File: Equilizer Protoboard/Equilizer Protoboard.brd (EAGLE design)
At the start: 14 parts, among them U1 ARDUINOR3-BPLACE

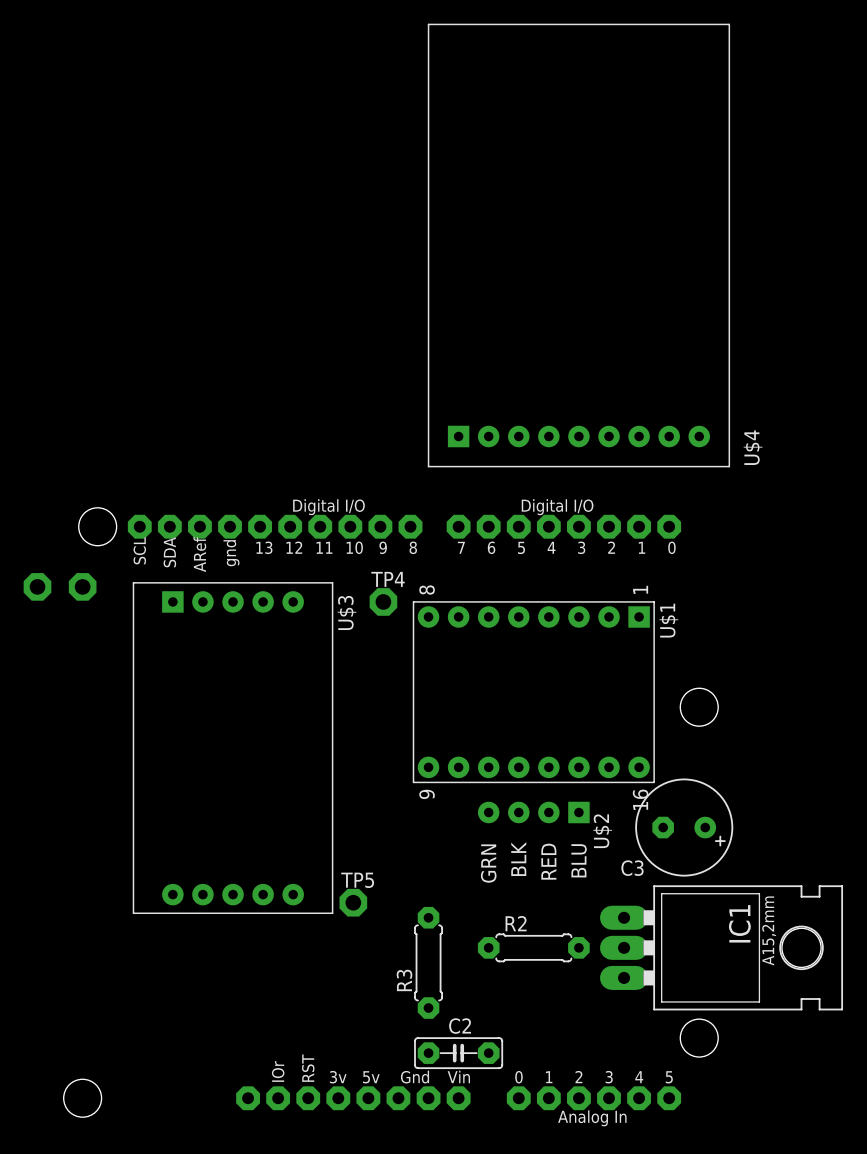
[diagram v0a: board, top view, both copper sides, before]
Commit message: Added Datalog Parser
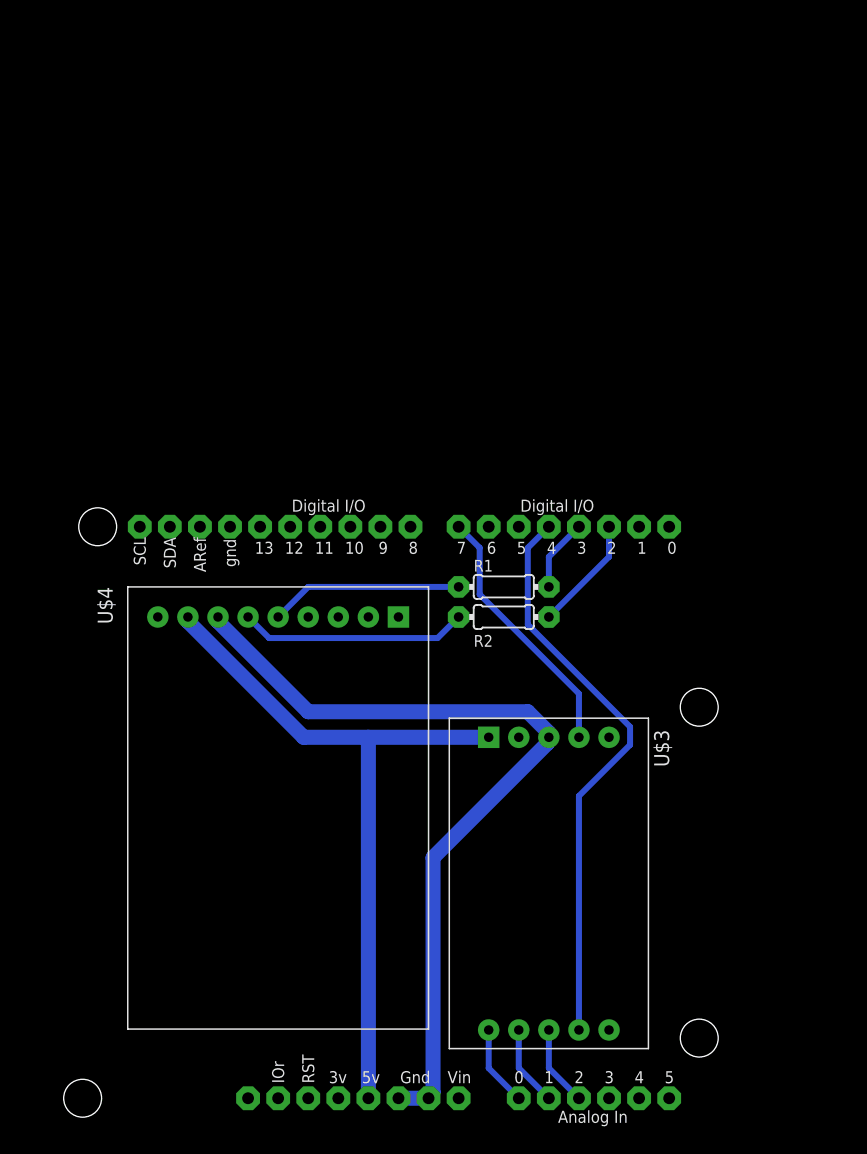
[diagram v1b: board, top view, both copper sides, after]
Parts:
- removed C2: 0.1uF, adafruit:C050-025X075
- removed C3: 1.0uF, adafruit:E3,5-8
- removed IC1: (no value), v-reg:317TL
- removed R3: 680, adafruit:0207/7
- removed TP11, TP12, TP4, TP5: TPPAD1-13, testpad:P1-13
- removed U$1: A4988, custom:A4988
- removed U$2: POLOLU_STEPPER, custom:POLOLU_STEPPER
- added R1: 0, adafruit:0204/7
- R2: value 330 -> 0; device adafruit:0207/7 -> adafruit:0204/7
- U1: device custom:ARDUINOR3-BPLACE -> adafruit:ARDUINOR3-BPLACE
- moved U$3 29.0 mm to (48.3, 33.0)
- moved R2 28.1 mm to (49.5, 43.2)
- moved U$4 16.1 mm to (40.6, 43.2), turned to 270 degrees
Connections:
- removed net N$13: TP5.TP, U$3.10
- removed net N$17: TP11.TP, U1.SCL
- removed net N$18: TP12.TP, U1.SDA
- removed net N$21: TP4.TP, U$3.5
- removed net N$22: IC1.1, R2.1, R3.2
- removed net N$29: U1.D5
- removed net N$6: U$1.12, U$2.3
- removed net N$7: U$1.11, U$2.4
- removed net VCC: C3.+, IC1.2, R2.2, U$1.16
- net +12V: no longer C2.1, IC1.3
- net +5V: no longer U$1.10
- net DIR: no longer U$1.8
- net GND: no longer C2.2, C3.-, U$1.15, U$1.9, U$3.3, U$4.7, U1.GND1, U1.GND2
- net N$1: now also U$3.3, U$4.7, U1.GND1, U1.GND2; no longer U$1.5, U$1.6
- net N$2: now also R2.1; no longer U1.D2
- net N$3: now also R1.1, U$4.5; no longer U$1.14, U$2.1
- net N$4: now also R1.2; no longer U$4.5
- net N$5: now also R2.2, U1.D2; no longer U$1.13, U$2.2
- net STEP: no longer U$1.7
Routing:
- net N$1: track 0.00 -> 69.8 mm
- net +5V: track 0.00 -> 60.3 mm
- net ACCEL_SLEEP: track 0.00 -> 48.6 mm
- net ACCEL_GS: track 0.00 -> 22.0 mm
- net N$2: track 0.00 -> 19.3 mm
- net N$3: track 0.00 -> 16.3 mm
- net N$5: track 0.00 -> 9.72 mm
- net N$11: track 0.00 -> 6.82 mm
- net N$12: track 0.00 -> 6.82 mm
- net N$10: track 0.00 -> 6.82 mm
- net N$4: track 0.00 -> 6.13 mm
